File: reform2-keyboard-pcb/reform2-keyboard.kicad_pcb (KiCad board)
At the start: 2 copper layers, 276 x 112.8 mm, 191 parts, among them J1 UART, J2 USB, J3 POWERCONN, J4 AUX, SW1 ML, SW10 ML, SW11 ML, SW12 ML, SW13 ML, SW14 ML, SW15 ML, SW16 ML, SW17 ML, SW18 ML, SW19 ML, SW2 ML, SW20 ML, SW21 ML, SW22 ML, SW23 ML, SW24 ML, SW25 ML, SW26 ML, SW27 ML, SW28 ML, SW29 ML, SW3 ML, SW30 ML, SW31 ML, SW32 ML, SW33 ML, SW34 ML, SW35 ML, SW36 ML, SW37 ML, SW38 ML, SW39 ML, SW4 ML, SW40 ML, SW41 ML, SW42 ML, SW43 ML, SW44 ML, SW45 ML, SW46 ML, SW47 ML, SW48 ML, SW49 ML, SW5 ML, SW50 ML, SW51 ML, SW52 ML, SW53 ML, SW54 ML, SW55 ML, SW56 ML, SW57 ML, SW58 ML, SW59 ML, SW6 ML, SW60 ML, SW61 ML, SW62 ML, SW63 ML, SW64 ML, SW65 ML, SW66 ML, SW67 ML, SW68 ML, SW69 ML, SW7 ML, SW70 ML, SW71 ML, SW72 ML, SW73 ML, SW74 ML, SW75 ML, SW76 ML, SW77 ML, SW78 ML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

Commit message: reform2.0 d-2 keyboard snapshot
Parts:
- removed J3: POWERCONN, Connector_PinHeader_2.54mm:PinHeader_1x03_P2.54mm_Horizontal
- removed R7: 0, Resistor_SMD:R_0603_1608Metric_Pad1.05x0.95mm_HandSolder
- removed SW90: POWER, Button_Switch_THT:SW_E-Switch_EG1271_DPDT
- removed U2: SM351LT, Package_TO_SOT_SMD:SOT-23
- added C6: 0.1uF, Capacitor_SMD:C_0603_1608Metric_Pad1.05x0.95mm_HandSolder, B.Cu at (150.2, 27.6)
- added H5: MH5, MountingHole:MountingHole_2.2mm_M2_Pad, F.Cu at (41.5, 25.1)
- added H6: MH6, MountingHole:MountingHole_2.2mm_M2_Pad, F.Cu at (244.4, 25.1)
- added R5: 4.7k, Resistor_SMD:R_0603_1608Metric, F.Cu at (202.4, 23.1)
- added TP1: TestPoint, TestPoint:TestPoint_Pad_D1.0mm, B.Cu at (153.6, 27.6)
- D1, D10, D11, D12, D13, D14, D15, D16, D17, D18, D19, D2, D20, D21, D22, D23, D24, D25, D26, D27, D28, D29, D3, D30, D31, D32, D33, D34, D35, D36, D37, D38, D39, D4, D40, D41, D42, D43, D44, D45, D46, D47, D48, D49, D5, D50, D51, D52, D53, D54, D55, D56, D57, D58, D59, D6, D60, D61, D62, D63, D64, D65, D66, D67, D68, D69, D7, D70, D71, D72, D73, D74, D75, D76, D77, D78, D79, D8, D80, D81, D82, D9: value D_Small -> MMDL914T1G
- J4: moved to F.Cu
- R1, R2: value 0 -> 22
- R6: value 0 -> 4.7k; footprint Resistor_SMD:R_0603_1608Metric_Pad1.05x0.95mm_HandSolder -> Resistor_SMD:R_0603_1608Metric; moved to F.Cu
- SW1, SW10, SW11, SW12, SW13, SW14, SW15, SW16, SW17, SW18, SW19, SW2, SW20, SW21, SW22, SW23, SW24, SW25, SW26, SW27, SW28, SW29, SW3, SW30, SW31, SW32, SW33, SW34, SW35, SW36, SW37, SW38, SW39, SW4, SW40, SW41, SW42, SW43, SW44, SW45, SW46, SW47, SW48, SW49, SW5, SW50, SW51, SW52, SW53, SW54, SW55, SW56, SW57, SW58, SW59, SW6, SW60, SW61, SW62, SW63, SW64, SW65, SW66, SW67, SW68, SW69, SW7, SW70, SW71, SW72, SW73, SW74, SW75, SW76, SW77, SW78, SW79, SW8, SW80, SW81, SW82, SW9: value ML -> Choc
- moved J4 100.6 mm to (196.5, 28.0)
- moved SW92 97.7 mm to (68.5, 26.8)
- moved SW91 95.6 mm to (59.4, 26.8)
- moved R6 84.8 mm to (202.4, 26.8), turned to 90 degrees
- moved GFX2 60.7 mm to (170.4, 25.8)
- moved GFX1 60.7 mm to (170.4, 25.8)
- moved J2 35.3 mm to (79.3, 22.0)
- moved J1 33.7 mm to (209.5, 28.0)
- moved R2 31.3 mm to (86.4, 25.4)
- moved R1 31.3 mm to (86.4, 27.4)
- moved C5 20.2 mm to (138.5, 40.7)
- moved H3 5.00 mm to (7.20, 121.0)
- moved H4 5.00 mm to (278.7, 121.0)
- moved D74 4.75 mm to (103.2, 129.9)
- moved SW75 4.70 mm to (128.8, 126.2)
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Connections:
- C4 pad 1: +5V -> +3V3
- J1 pad 1: +5V -> +3V3
- J2 pad 1: Net-(J2-Pad1) -> +5V
- J4 pad 1: +5V -> +3V3
- J4 pad 2: AUX2 -> DISP_SCL
- J4 pad 3: AUX1 -> DISP_SDA
- R3 pad 1: +5V -> +3V3
- R4 pad 2: +5V -> +3V3
- R6 pad 1: +5V -> +3V3
- R6 pad 2: Net-(J2-Pad1) -> DISP_SCL
- U1 pad 12: AUX2 -> UART_TX
- U1 pad 14: +5V -> +3V3
- U1 pad 18: UART_TX -> DISP_SCL
- U1 pad 19: COL4 -> DISP_SDA
- U1 pad 24: +5V -> +3V3
- U1 pad 32: AUX1 -> COL4
- U1 pad 34: +5V -> +3V3
- U1 pad 36: LID_SENSE -> AUX
- U1 pad 44: +5V -> +3V3
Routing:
- net +5V: track 227.2 -> 86.2 mm, vias 8 -> 3
- net GND: track 609.2 -> 478.8 mm, vias 28 -> 27
- net +3V3: track 0.00 -> 128.6 mm, vias 0 -> 2
- net PROG: track 15.9 -> 92.2 mm
- net DISP_SCL: track 0.00 -> 68.4 mm, vias 0 -> 1
- net DISP_SDA: track 0.00 -> 67.3 mm, vias 0 -> 1
- net LID_SENSE: track 58.9 -> 0.00 mm, vias 1 -> 0
- net AUX1: track 57.1 -> 0.00 mm, vias 1 -> 0
- net RESET: track 30.7 -> 81.6 mm
- net AUX2: track 42.3 -> 0.00 mm, vias 1 -> 0
- net UART_TX: track 40.1 -> 80.9 mm
- net UART_RX: track 42.6 -> 80.6 mm, vias 2 -> 1
- net /Reform KBD MCU/UD-: track 25.9 -> 57.8 mm
- net /Reform KBD MCU/UD+: track 24.6 -> 56.4 mm
- net PWRIN: track 25.3 -> 0.00 mm
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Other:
- board size 276 x 112.8 mm -> 275.9 x 112.8 mm
- board text added: "GND SDA SCL 3V3"
- board text added: "GND TX RX 3V3"
- board text added: "MNT Reform 2 Keyboard Rev D-2 MNT Research GmbH 2019-05-31 GPLv3+ mntre.com"
- board text removed: "5V AUX2 AUX1 GND"
- board text removed: "FLASH"
- board text removed: "GND"
- board text removed: "GND TX RX 5V"
- board text removed: "MNT Reform 2.0 Keyboard Rev D-2019-05-31 (C) 2019 MNT Research GmbH GPLv3+ https://mntre.com"
- board text removed: "POWER"
- board text removed: "PWRIN (5V)"
- board text removed: "PWROUT"
- board text removed: "RESET"

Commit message: Reform2.0D-3 snapshot of PCBs and input device firmware
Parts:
- removed TP1: TestPoint, TestPoint:TestPoint_Pad_D1.0mm
- added C10: 4.7uF, Capacitor_SMD:C_0603_1608Metric, F.Cu at (69.2, 23.0)
- added C7: 4.7uF, Capacitor_SMD:C_0603_1608Metric, F.Cu at (59.2, 24.8)
- added C8: 1uF, Capacitor_SMD:C_0603_1608Metric, F.Cu at (61.2, 21.8)
- added C9: 1uF, Capacitor_SMD:C_0603_1608Metric, F.Cu at (57.8, 22.8)
- added D100: WLED, LED_SMD:LED_0603_1608Metric, F.Cu at (54.8, 51.0)
- added D101: WLED, LED_SMD:LED_0603_1608Metric, F.Cu at (73.5, 51.0)
- added D102: WLED, LED_SMD:LED_0603_1608Metric, F.Cu at (92.0, 51.0)
- added D103: WLED, LED_SMD:LED_0603_1608Metric, F.Cu at (110.5, 51.0)
- added D104: WLED, LED_SMD:LED_0603_1608Metric, F.Cu at (129.0, 51.0)
- added D105: WLED, LED_SMD:LED_0603_1608Metric, F.Cu at (147.8, 51.0)
- added D106: WLED, LED_SMD:LED_0603_1608Metric, F.Cu at (166.2, 51.0)
- added D107: WLED, LED_SMD:LED_0603_1608Metric, F.Cu at (184.8, 51.0)
- added D108: WLED, LED_SMD:LED_0603_1608Metric, F.Cu at (203.5, 51.0)
- added D109: WLED, LED_SMD:LED_0603_1608Metric, F.Cu at (222.0, 51.0)
- added D110: WLED, LED_SMD:LED_0603_1608Metric, F.Cu at (240.8, 51.0)
- added D111: WLED, LED_SMD:LED_0603_1608Metric, F.Cu at (263.8, 51.0)
- added D112: WLED, LED_SMD:LED_0603_1608Metric, F.Cu at (22.0, 68.8)
- added D113: WLED, LED_SMD:LED_0603_1608Metric, F.Cu at (45.0, 68.8)
- added D114: WLED, LED_SMD:LED_0603_1608Metric, F.Cu at (63.8, 68.8)
- added D115: WLED, LED_SMD:LED_0603_1608Metric, F.Cu at (82.2, 68.8)
- added D116: WLED, LED_SMD:LED_0603_1608Metric, F.Cu at (101.0, 68.8)
- added D117: WLED, LED_SMD:LED_0603_1608Metric, F.Cu at (119.5, 68.8)
- added D118: WLED, LED_SMD:LED_0603_1608Metric, F.Cu at (138.0, 68.8)
- added D119: WLED, LED_SMD:LED_0603_1608Metric, F.Cu at (156.8, 68.8)
- added D120: WLED, LED_SMD:LED_0603_1608Metric, F.Cu at (175.2, 68.8)
- added D121: WLED, LED_SMD:LED_0603_1608Metric, F.Cu at (194.0, 68.8)
- added D122: WLED, LED_SMD:LED_0603_1608Metric, F.Cu at (212.5, 68.8)
- added D123: WLED, LED_SMD:LED_0603_1608Metric, F.Cu at (231.2, 68.8)
- added D124: WLED, LED_SMD:LED_0603_1608Metric, F.Cu at (249.8, 68.8)
- added D125: WLED, LED_SMD:LED_0603_1608Metric, F.Cu at (268.5, 68.8)
- added D126: WLED, LED_SMD:LED_0603_1608Metric, F.Cu at (17.5, 86.2)
- added D127: WLED, LED_SMD:LED_0603_1608Metric, F.Cu at (36.0, 86.2)
- added D128: WLED, LED_SMD:LED_0603_1608Metric, F.Cu at (54.8, 86.2)
- added D129: WLED, LED_SMD:LED_0603_1608Metric, F.Cu at (73.2, 86.2)
- added D130: WLED, LED_SMD:LED_0603_1608Metric, F.Cu at (92.0, 86.2)
- added D131: WLED, LED_SMD:LED_0603_1608Metric, F.Cu at (110.5, 86.2)
- added D132: WLED, LED_SMD:LED_0603_1608Metric, F.Cu at (129.2, 86.2)
- added D133: WLED, LED_SMD:LED_0603_1608Metric, F.Cu at (147.8, 86.2)
- added D134: WLED, LED_SMD:LED_0603_1608Metric, F.Cu at (166.5, 86.2)
- added D135: WLED, LED_SMD:LED_0603_1608Metric, F.Cu at (185.0, 86.2)
- added D136: WLED, LED_SMD:LED_0603_1608Metric, F.Cu at (203.5, 86.2)
- added D137: WLED, LED_SMD:LED_0603_1608Metric, F.Cu at (222.2, 86.2)
- added D138: WLED, LED_SMD:LED_0603_1608Metric, F.Cu at (240.8, 86.2)
- added D139: WLED, LED_SMD:LED_0603_1608Metric, F.Cu at (263.8, 86.2)
- added D140: WLED, LED_SMD:LED_0603_1608Metric, F.Cu at (22.0, 103.8)
- added D141: WLED, LED_SMD:LED_0603_1608Metric, F.Cu at (45.0, 103.8)
- added D142: WLED, LED_SMD:LED_0603_1608Metric, F.Cu at (63.8, 103.8)
- added D143: WLED, LED_SMD:LED_0603_1608Metric, F.Cu at (82.2, 104.0)
- added D144: WLED, LED_SMD:LED_0603_1608Metric, F.Cu at (101.0, 103.8)
- added D145: WLED, LED_SMD:LED_0603_1608Metric, F.Cu at (119.5, 103.8)
- added D146: WLED, LED_SMD:LED_0603_1608Metric, F.Cu at (138.0, 103.8)
- added D147: WLED, LED_SMD:LED_0603_1608Metric, F.Cu at (156.8, 103.8)
- added D148: WLED, LED_SMD:LED_0603_1608Metric, F.Cu at (175.5, 103.8)
- added D149: WLED, LED_SMD:LED_0603_1608Metric, F.Cu at (194.0, 103.8)
- added D150: WLED, LED_SMD:LED_0603_1608Metric, F.Cu at (212.8, 103.8)
- added D151: WLED, LED_SMD:LED_0603_1608Metric, F.Cu at (231.2, 103.8)
- added D152: WLED, LED_SMD:LED_0603_1608Metric, F.Cu at (249.8, 103.8)
- added D153: WLED, LED_SMD:LED_0603_1608Metric, F.Cu at (268.5, 103.8)
- added D154: WLED, LED_SMD:LED_0603_1608Metric, F.Cu at (22.0, 121.5)
- added D155: WLED, LED_SMD:LED_0603_1608Metric, F.Cu at (49.8, 121.5)
- added D156: WLED, LED_SMD:LED_0603_1608Metric, F.Cu at (77.8, 121.5)
- added D157: WLED, LED_SMD:LED_0603_1608Metric, F.Cu at (128.8, 121.5)
- added D158: WLED, LED_SMD:LED_0603_1608Metric, F.Cu at (147.5, 121.5)
- added D159: WLED, LED_SMD:LED_0603_1608Metric, F.Cu at (194.0, 121.5)
- added D160: WLED, LED_SMD:LED_0603_1608Metric, F.Cu at (212.5, 121.5)
- added D161: WLED, LED_SMD:LED_0603_1608Metric, F.Cu at (231.2, 121.5)
- added D162: WLED, LED_SMD:LED_0603_1608Metric, F.Cu at (249.7, 121.5)
- added D163: WLED, LED_SMD:LED_0603_1608Metric, F.Cu at (268.2, 121.5)
- added D83: B250-13-F, Diode_SMD:D_SMB_Handsoldering, F.Cu at (65.5, 27.2)
- added D84: WLED, LED_SMD:LED_0603_1608Metric, F.Cu at (17.5, 33.5)
- added D85: WLED, LED_SMD:LED_0603_1608Metric, F.Cu at (36.0, 33.5)
- added D86: WLED, LED_SMD:LED_0603_1608Metric, F.Cu at (54.8, 33.5)
- added D87: WLED, LED_SMD:LED_0603_1608Metric, F.Cu at (73.2, 33.5)
- added D88: WLED, LED_SMD:LED_0603_1608Metric, F.Cu at (92.0, 33.5)
- added D89: WLED, LED_SMD:LED_0603_1608Metric, F.Cu at (110.5, 33.5)
- added D90: WLED, LED_SMD:LED_0603_1608Metric, F.Cu at (129.2, 33.5)
- added D91: WLED, LED_SMD:LED_0603_1608Metric, F.Cu at (147.8, 33.5)
- added D92: WLED, LED_SMD:LED_0603_1608Metric, F.Cu at (166.2, 33.5)
- added D93: WLED, LED_SMD:LED_0603_1608Metric, F.Cu at (185.0, 33.5)
- added D94: WLED, LED_SMD:LED_0603_1608Metric, F.Cu at (203.5, 33.5)
- added D95: WLED, LED_SMD:LED_0603_1608Metric, F.Cu at (222.2, 33.5)
- added D96: WLED, LED_SMD:LED_0603_1608Metric, F.Cu at (240.8, 33.5)
- added D97: WLED, LED_SMD:LED_0603_1608Metric, F.Cu at (263.8, 33.5)
- added D98: WLED, LED_SMD:LED_0603_1608Metric, F.Cu at (17.5, 51.0)
- added D99: WLED, LED_SMD:LED_0603_1608Metric, F.Cu at (36.0, 51.0)
- added J4: USB_C_Receptacle_USB2.0, Connector_USB:USB_C_Receptacle_Amphenol_12401610E4-2A, F.Cu at (92.0, 24.0)
- added L1: 10uH, reform2-keyboard:IND_SRP4020TA-150M, F.Cu at (65.2, 22.2)
- added R10: 715K, Resistor_SMD:R_0603_1608Metric, F.Cu at (53.2, 21.8)
- added R11: 1M, Resistor_SMD:R_0603_1608Metric, F.Cu at (64.0, 30.2)
- added R12: 54.9K, Resistor_SMD:R_0603_1608Metric, F.Cu at (64.0, 32.0)
- added R13: 5.1k, Resistor_SMD:R_0603_1608Metric, F.Cu at (98.4, 28.4)
- added R14: 5.1k, Resistor_SMD:R_0603_1608Metric, F.Cu at (85.5, 28.4)
- added R7: 62K, Resistor_SMD:R_0603_1608Metric, F.Cu at (50.0, 28.0)
- added R8: 604K, Resistor_SMD:R_0603_1608Metric, F.Cu at (55.0, 21.8)
- added R9: 0, Resistor_SMD:R_0603_1608Metric, F.Cu at (57.8, 21.0)
- added U2: TPS61185, Package_DFN_QFN:VQFN-24-1EP_4x4mm_P0.5mm_EP2.45x2.45mm, F.Cu at (54.8, 26.5)
- C1, C2, C3, C6: footprint Capacitor_SMD:C_0603_1608Metric_Pad1.05x0.95mm_HandSolder -> Capacitor_SMD:C_0603_1608Metric
- C4: renamed from C5; footprint Capacitor_SMD:C_0603_1608Metric_Pad1.05x0.95mm_HandSolder -> Capacitor_SMD:C_0603_1608Metric
- C5: renamed from C4; footprint Capacitor_SMD:C_0603_1608Metric_Pad1.05x0.95mm_HandSolder -> Capacitor_SMD:C_0603_1608Metric
- J1: renamed from J2; footprint Connector_PinHeader_2.00mm:PinHeader_1x04_P2.00mm_Horizontal -> Connector_JST:JST_PH_S4B-PH-SM4-TB_1x04-1MP_P2.00mm_Horizontal; moved to F.Cu
- J2: renamed from J1; footprint Connector_PinHeader_2.00mm:PinHeader_1x04_P2.00mm_Horizontal -> Connector_JST:JST_PH_S4B-PH-SM4-TB_1x04-1MP_P2.00mm_Horizontal; moved to F.Cu
- J3: renamed from J4; footprint Connector_PinHeader_2.00mm:PinHeader_1x04_P2.00mm_Horizontal -> Connector_FFC-FPC:Molex_200528-0040_1x04-1MP_P1.00mm_Horizontal
- R1, R2: footprint Resistor_SMD:R_0603_1608Metric_Pad1.05x0.95mm_HandSolder -> Resistor_SMD:R_0603_1608Metric; moved to F.Cu
- R3, R4: footprint Resistor_SMD:R_0603_1608Metric_Pad1.05x0.95mm_HandSolder -> Resistor_SMD:R_0603_1608Metric
- moved SW83 55.9 mm to (115.2, 23.8)
- moved SW84 38.1 mm to (106.5, 23.8)
- moved R2 33.6 mm to (119.9, 27.6)
- moved R1 33.5 mm to (119.9, 29.2)
- moved R5 15.5 mm to (187.0, 24.5), turned to 90 degrees
- moved R6 15.5 mm to (187.0, 28.0), turned to 270 degrees
- moved J1 3.72 mm to (77.5, 25.2)
- moved R3 3.25 mm to (125.8, 29.2), turned to 180 degrees
- moved GFX2 2.96 mm to (167.5, 25.2)
- moved GFX1 2.93 mm to (167.5, 25.2)
- moved J2 2.93 mm to (208.5, 25.2), turned to 180 degrees
- moved J3 2.51 mm to (194.0, 28.2)
- moved C4 2.44 mm to (137.5, 38.5), turned to 270 degrees
- moved C3 1.15 mm to (134.0, 35.8), turned to 180 degrees
- turned C6 to 315 degrees
- renumbered D44 to D10, D58 to D11, D72 to D12, D3 to D13, D17 to D14, D31 to D15, D45 to D16, D59 to D17, D73 to D18, D4 to D19, D15 to D2, D18 to D20, D32 to D21, D46 to D22, D60 to D23, D74 to D24, D5 to D25, D19 to D26, D33 to D27, D47 to D28, D61 to D29, D29 to D3, D75 to D30, D6 to D31, D20 to D32, D34 to D33, D48 to D34, D62 to D35, D76 to D36, D7 to D37, D21 to D38, D35 to D39, D43 to D4, D49 to D40, D63 to D41, D77 to D42, D8 to D43, D22 to D44, D36 to D45, D50 to D46, D64 to D47, D78 to D48, D9 to D49, D57 to D5, D23 to D50, D37 to D51, D51 to D52, D65 to D53, D79 to D54, D10 to D55, D24 to D56, D38 to D57, D52 to D58, D66 to D59, D71 to D6, D80 to D60, D11 to D61, D25 to D62, D39 to D63, D53 to D64, D67 to D65, D81 to D66, D12 to D67, D26 to D68, D40 to D69, D2 to D7, D54 to D70, D68 to D71, D82 to D72, D13 to D73, D27 to D74, D41 to D75, D55 to D76, D69 to D77, D14 to D78, D28 to D79, D16 to D8, D42 to D80, D56 to D81, D70 to D82, D30 to D9, SW44 to SW10, SW58 to SW11, SW72 to SW12, SW3 to SW13, SW17 to SW14, SW31 to SW15, SW45 to SW16, SW59 to SW17, SW73 to SW18, SW4 to SW19, SW15 to SW2, SW18 to SW20, SW32 to SW21, SW46 to SW22, SW60 to SW23, SW74 to SW24, SW5 to SW25, SW19 to SW26, SW33 to SW27, SW47 to SW28, SW61 to SW29, SW29 to SW3, SW75 to SW30, SW6 to SW31, SW20 to SW32, SW34 to SW33, SW48 to SW34, SW62 to SW35, SW76 to SW36, SW7 to SW37, SW21 to SW38, SW35 to SW39, SW43 to SW4, SW49 to SW40, SW63 to SW41, SW77 to SW42, SW8 to SW43, SW22 to SW44, SW36 to SW45, SW50 to SW46, SW64 to SW47, SW78 to SW48, SW9 to SW49, SW57 to SW5, SW23 to SW50, SW37 to SW51, SW51 to SW52, SW65 to SW53, SW79 to SW54, SW10 to SW55, SW24 to SW56, SW38 to SW57, SW52 to SW58, SW66 to SW59, SW71 to SW6, SW80 to SW60, SW11 to SW61, SW25 to SW62, SW39 to SW63, SW53 to SW64, SW67 to SW65, SW81 to SW66, SW12 to SW67, SW26 to SW68, SW40 to SW69, SW2 to SW7, SW54 to SW70, SW68 to SW71, SW82 to SW72, SW13 to SW73, SW27 to SW74, SW41 to SW75, SW55 to SW76, SW69 to SW77, SW14 to SW78, SW28 to SW79, SW16 to SW8, SW42 to SW80, SW56 to SW81, SW70 to SW82, SW91 to SW83, SW92 to SW84, SW30 to SW9
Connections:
- U1 pad 1: UART_RX -> COL3
- U1 pad 12: UART_TX -> PWM
- U1 pad 20: COL3 -> UART_RX
- U1 pad 21: COL2 -> UART_TX
- U1 pad 36: AUX -> COL2
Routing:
- net Net-(C10-Pad1): track 0.00 -> 530.4 mm, vias 0 -> 14
- net GND: track 478.8 -> 107.7 mm, vias 27 -> 68
- net Net-(D163-Pad1): track 0.00 -> 321.2 mm, vias 0 -> 4
- net Net-(D153-Pad1): track 0.00 -> 299.3 mm, vias 0 -> 6
- net Net-(D97-Pad1): track 0.00 -> 273.8 mm, vias 0 -> 2
- net Net-(D125-Pad1): track 0.00 -> 271.3 mm, vias 0 -> 2
- net Net-(D111-Pad1): track 0.00 -> 263.0 mm, vias 0 -> 2
- net Net-(D139-Pad1): track 0.00 -> 262.8 mm, vias 0 -> 2
- net Net-(D123-Pad1): track 0.00 -> 224.9 mm, vias 0 -> 2
- net Net-(D133-Pad1): track 0.00 -> 171.8 mm, vias 0 -> 2
- net Net-(D93-Pad1): track 0.00 -> 166.6 mm, vias 0 -> 6
- net Net-(D143-Pad1): track 0.00 -> 123.3 mm, vias 0 -> 2
- net PWM: track 0.00 -> 92.3 mm, vias 0 -> 4
- net Net-(D103-Pad1): track 0.00 -> 76.6 mm, vias 0 -> 2
- net +5V: track 86.2 -> 150.2 mm, vias 3 -> 10
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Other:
- board text added: "MNT REFORM KEYBOARD 2.0D-3 2020-03-05 MNTRE.COM"
- board text added: "OLED"
- board text added: "PROG"
- board text added: "RST"
- board text added: "UART"
- board text removed: "5V D- D+ GND"
- board text removed: "GND SDA SCL 3V3"
- board text removed: "GND TX RX 3V3"
- board text removed: "MNT Reform 2 Keyboard Rev D-2 MNT Research GmbH 2019-05-31 GPLv3+ mntre.com"

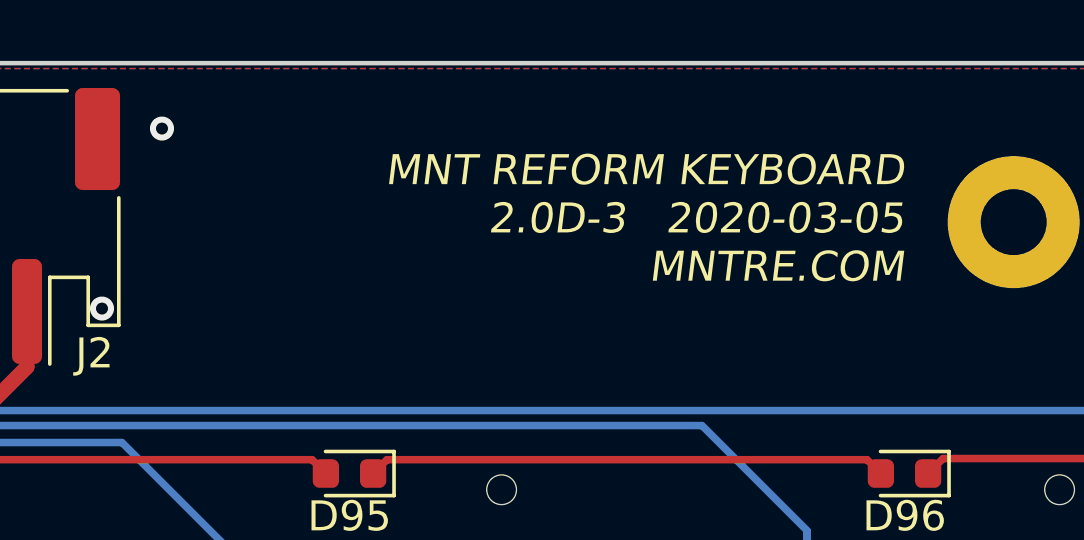
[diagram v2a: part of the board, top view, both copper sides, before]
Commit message: WIP keyboard now CERN-OHL-S 2.0
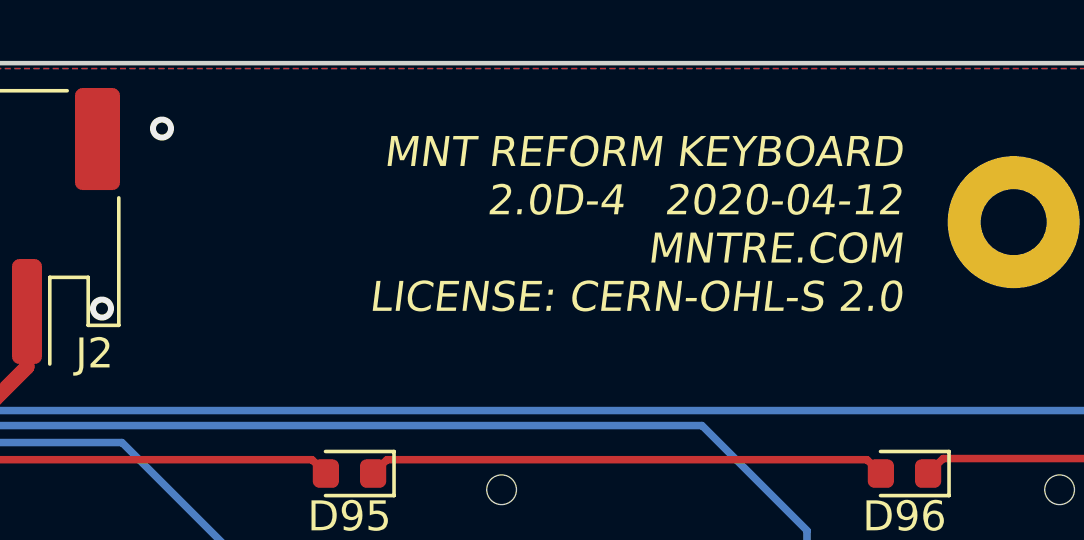
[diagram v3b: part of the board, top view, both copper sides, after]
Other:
- board text added: "MNT REFORM KEYBOARD 2.0D-4 2020-04-12 MNTRE.COM LICENSE: CERN-OHL-S 2.0"
- board text removed: "MNT REFORM KEYBOARD 2.0D-3 2020-03-05 MNTRE.COM"
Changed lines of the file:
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@@
-(kicad_pcb (version 20171130) (host pcbnew 5.1.2+dfsg1-1)
+(kicad_pcb (version 20171130) (host pcbnew 5.1.5+dfsg1-2+b1)
   (general
     (thickness 1.6)
@@
   )
   (gr_line (start 5 31.24) (end 5.5 30.74) (layer Edge.Cuts) (width 0.15))
-  (gr_text "MNT REFORM KEYBOARD\n2.0D-3   2020-03-05\nMNTRE.COM" (at 240.75 25) (layer F.SilkS)
+  (gr_text "MNT REFORM KEYBOARD\n2.0D-4   2020-04-12\nMNTRE.COM\nLICENSE: CERN-OHL-S 2.0" (at 240.7 25.2) (layer F.SilkS)
     (effects (font (size 1 1) (thickness 0.15) italic) (justify right))
   )

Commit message: reform2-keyboard: version 2d5; add info badge; finalize connector positions; add optional 3v3 regulator for standalone
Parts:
- added C11: 1uF, Capacitor_SMD:C_0603_1608Metric, F.Cu at (153.0, 29.4)
- added C12: 1uF, Capacitor_SMD:C_0603_1608Metric, F.Cu at (152.4, 25.3)
- added G***: LOGO, reform2-keyboard:mntreform-keyboard-badge, F.Cu at (114.9, 24.9)
- added U3: MCP1700-3302E_SOT23, Package_TO_SOT_SMD:SOT-23, F.Cu at (154.5, 27.1)
- Y1: footprint Crystals:Crystal_SMD_3225-4pin_3.2x2.5mm_HandSoldering -> Crystal:Crystal_SMD_3225-4Pin_3.2x2.5mm
- moved J1 144.5 mm to (222.0, 26.0)
- moved J2 131.0 mm to (77.5, 26.0)
- moved J4 117.0 mm to (208.9, 20.5)
- moved R14 117.0 mm to (202.4, 24.9)
- moved R13 113.8 mm to (212.2, 27.5), turned to 180 degrees
- moved R1 68.8 mm to (188.2, 20.9), turned to 0 degrees
- moved R2 68.5 mm to (188.2, 22.4), turned to 0 degrees
- moved SW83 23.5 mm to (92.0, 27.0)
- moved SW84 14.5 mm to (92.0, 22.8)
- moved C1 4.14 mm to (126.8, 24.3), turned to 45 degrees
- moved GFX1 3.71 mm to (171.2, 25.1)
- moved J3 3.48 mm to (196.0, 25.4), turned to 270 degrees
- moved R6 2.68 mm to (188.2, 25.6), turned to 180 degrees
- moved Y1 1.93 mm to (128.7, 26.3), turned to 45 degrees
- moved C5 1.41 mm to (145.1, 20.9)
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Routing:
- net +5V: track 150.2 -> 236.9 mm, vias 10 -> 11
- net /Reform KBD MCU/UD+: track 21.6 -> 61.5 mm
- net +3V3: track 126.3 -> 165.6 mm, vias 4 -> 6
- net /Reform KBD MCU/UD-: track 23.0 -> 60.6 mm
- net PROG: track 52.9 -> 76.1 mm, vias 1 -> 3
- net RESET: track 25.2 -> 47.9 mm
- net UART_TX: track 81.8 -> 68.9 mm, vias 3 -> 1
- net UART_RX: track 76.8 -> 65.8 mm, vias 3 -> 1
- net D+: track 59.0 -> 53.6 mm
- net D-: track 57.2 -> 51.8 mm
- net COL1: track 234.5 -> 239.4 mm
- net Net-(J4-PadA5): track 6.82 -> 2.95 mm
- net COL2: track 242.2 -> 245.2 mm
- net Net-(C2-Pad1): track 8.45 -> 6.41 mm
- net COL14: track 207.0 -> 209.0 mm
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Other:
- board size 275.9 x 112.8 mm -> 275.9 x 117.8 mm
- board text added: "USB"
- board text removed: "MNT REFORM KEYBOARD 2.0D-4 2020-04-12 MNTRE.COM LICENSE: CERN-OHL-S 2.0"

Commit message: place left side
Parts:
- removed D12, D18, D24, D30, D36, D42, D48, D54, D6, D60, D66, D72, D73, D74, D75, D76, D77, D78, D79, D80, D81, D82: MMDL914T1G, Diode_SMD:D_0603_1608Metric_Pad1.05x0.95mm_HandSolder
- removed D154, D155, D156, D157, D158, D159, D160, D161, D162, D163: WLED, LED_SMD:LED_0603_1608Metric
- removed G***: LOGO, reform2-keyboard:mntreform-keyboard-badge
- removed SW12, SW18, SW24, SW30, SW36, SW42, SW48, SW54, SW6, SW60, SW66, SW72, SW73, SW74, SW75, SW76, SW77, SW78, SW79, SW80, SW81, SW82: Choc, keyswitches:PG1350
- C1, C2, C3, C4, C5, C6, R3, R4, U1, Y1: moved to F.Cu
- moved D97 203.3 mm to (69.4, 93.1), turned to 173 degrees
- moved D96 174.3 mm to (71.5, 75.3), turned to 173 degrees
- moved D133 172.9 mm to (1.95, -6.63)
- moved D95 150.6 mm to (73.6, 57.6), turned to 173 degrees
- moved D50 149.3 mm to (14.7, 50.8), turned to 354.5 degrees
- moved D111 138.1 mm to (128.8, 80.3), turned to 178.35 degrees
- moved D37 128.2 mm to (133.5, 170.9)
- moved D38 128.2 mm to (133.6, 188.5)
- moved D40 128.2 mm to (133.5, 223.7)
- moved D41 128.2 mm to (142.5, 241.3)
- moved D43 128.2 mm to (152.1, 170.9)
- moved D44 128.2 mm to (152.2, 188.5)
- moved D46 128.2 mm to (152.1, 223.7)
- moved D49 128.2 mm to (170.7, 170.9)
- moved D55 128.2 mm to (189.4, 170.9)
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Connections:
- J4 pad A8: Net-(J4-PadA8) -> (no net)
- J4 pad B8: Net-(J4-PadB8) -> (no net)
- U1 pad 25: ROW6 -> (no net)
- U1 pad 31: COL14 -> (no net)
- U1 pad 37: COL13 -> (no net)
- U2 pad 21: Net-(U2-Pad21) -> (no net)
- U2 pad 4: Net-(U2-Pad4) -> (no net)
- U2 pad 7: Net-(D163-Pad1) -> (no net)
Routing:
- net Net-(C10-Pad1): track 530.4 -> 0.00 mm, vias 14 -> 0
- net ROW6: track 382.3 -> 0.00 mm, vias 2 -> 0
- net ROW5: track 374.2 -> 0.00 mm, vias 2 -> 0
- net ROW4: track 351.5 -> 0.00 mm, vias 2 -> 0
- net ROW3: track 334.1 -> 0.00 mm, vias 2 -> 0
- net Net-(D163-Pad1): track 321.2 -> 0.00 mm, vias 4 -> 0
- net ROW2: track 313.9 -> 0.00 mm, vias 2 -> 0
- net Net-(D153-Pad1): track 299.3 -> 0.00 mm, vias 6 -> 0
- net ROW1: track 295.9 -> 0.00 mm, vias 2 -> 0
- net Net-(D97-Pad1): track 273.8 -> 0.00 mm, vias 2 -> 0
- net Net-(D125-Pad1): track 271.3 -> 0.00 mm, vias 2 -> 0
- net Net-(D111-Pad1): track 263.0 -> 0.00 mm, vias 2 -> 0
- net Net-(D139-Pad1): track 262.8 -> 0.00 mm, vias 2 -> 0
- net COL2: track 245.2 -> 0.00 mm, vias 4 -> 0
- net COL1: track 239.4 -> 0.00 mm
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
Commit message: first pass layout & routing
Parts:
- removed D124, D125, D126, D127, D128, D129, D130, D131, D132, D133: WLED, LED_SMD:LED_0603_1608Metric
- added D72: MMDL914T1G, reform2-keyboard:D_0603_1608Metric_Pad1.05x0.95mm_HandSolderPlusVias, F.Cu at (26.9, 36.1)
- added D73: MMDL914T1G, reform2-keyboard:D_0603_1608Metric_Pad1.05x0.95mm_HandSolderPlusVias, F.Cu at (259.8, 45.2)
- added SW72: Choc, keyswitches:PG1350, F.Cu at (17.5, 40.4)
- added SW73: Choc, keyswitches:PG1350, F.Cu at (268.5, 40.4)
- D1, D10, D11, D13, D14, D15, D16, D17, D19, D2, D20, D21, D22, D23, D25, D26, D27, D28, D29, D3, D31, D32, D33, D34, D35, D37, D38, D39, D4, D40, D41, D43, D44, D45, D46, D47, D49, D5, D50, D51, D52, D53, D55, D56, D57, D58, D59, D61, D62, D63, D64, D65, D67, D68, D69, D7, D70, D71, D8, D9: footprint Diode_SMD:D_0603_1608Metric_Pad1.05x0.95mm_HandSolder -> reform2-keyboard:D_0603_1608Metric_Pad1.05x0.95mm_HandSolderPlusVias; moved to F.Cu
- moved D140 213.3 mm to (216.6, 93.2), turned to 187 degrees
- moved D50 171.7 mm to (185.2, 71.4), turned to 96.2 degrees
- moved D61 141.7 mm to (221.0, 49.0), turned to 97 degrees
- moved D114 140.9 mm to (153.9, 44.5), turned to 181.65 degrees
- moved D141 135.0 mm to (214.4, 75.3), turned to 187 degrees
- moved D70 125.9 mm to (250.1, 100.1), turned to 95.5 degrees
- moved D71 125.3 mm to (256.8, 117.9), turned to 95.5 degrees
- moved D68 125.1 mm to (243.1, 64.5), turned to 95.5 degrees
- moved D67 125.1 mm to (241.3, 46.7), turned to 95.5 degrees
- moved D142 125.0 mm to (212.2, 57.4), turned to 187 degrees
- moved D69 123.9 mm to (244.6, 82.5), turned to 95.5 degrees
- moved D64 122.8 mm to (227.6, 102.6), turned to 97 degrees
- moved D62 122.7 mm to (223.3, 66.8), turned to 97 degrees
- moved D63 121.8 mm to (225.3, 84.6), turned to 97 degrees
- moved D65 121.7 mm to (233.8, 120.8), turned to 97 degrees
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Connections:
- U1 pad 25: (no net) -> ROW6
- U2 pad 10: Net-(D133-Pad1) -> (no net)
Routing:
- net ROW5: track 0.00 -> 363.0 mm, vias 0 -> 2
- net ROW4: track 0.00 -> 331.7 mm, vias 0 -> 2
- net ROW3: track 0.00 -> 311.2 mm, vias 0 -> 2
- net ROW2: track 0.00 -> 290.5 mm, vias 0 -> 1
- net ROW6: track 0.00 -> 267.7 mm, vias 0 -> 2
- net ROW1: track 0.00 -> 265.2 mm, vias 0 -> 1
- net Net-(D153-Pad1): track 0.00 -> 260.8 mm, vias 0 -> 2
- net Net-(C10-Pad1): track 0.00 -> 246.0 mm, vias 0 -> 6
- net COL11: track 0.00 -> 216.0 mm, vias 0 -> 1
- net +5V: track 0.00 -> 215.4 mm, vias 0 -> 6
- net COL12: track 0.00 -> 212.1 mm, vias 0 -> 1
- net COL1: track 0.00 -> 201.2 mm, vias 0 -> 2
- net COL2: track 0.00 -> 178.8 mm, vias 0 -> 2
- net Net-(D143-Pad1): track 0.00 -> 178.7 mm, vias 0 -> 4
- net +3V3: track 0.00 -> 178.7 mm, vias 0 -> 9
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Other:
- net class Power: trace_width 0.5 -> 0.25; via_dia 1 -> 0.8; via_drill 0.6 -> 0.4
- net class skinny added: clearance 0.2, trace_width 0.2, via_dia 0.8, via_drill 0.4

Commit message: finish manual routing
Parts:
- moved R3 2.92 mm to (121.9, 27.2)
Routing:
- net RESET: track 58.7 -> 55.0 mm
- net +3V3: track 178.7 -> 180.3 mm
- net DISP_SCL: track 68.6 -> 69.9 mm
- net PWM: track 94.2 -> 93.1 mm
- net DISP_SDA: track 69.9 -> 70.8 mm
- net GND: track 48.7 -> 49.6 mm, vias 21 -> 23
- net COL6: track 138.3 -> 138.9 mm
- net COL5: track 136.1 -> 136.6 mm
